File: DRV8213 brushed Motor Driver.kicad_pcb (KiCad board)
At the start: 4 copper layers, 15 x 15 mm, 27 parts, among them J1 Keystone 6102, J10 Precidip 852-10-004-20-001101, J11 Precidip 852-10-004-20-001101, J2 Keystone 6102, J3 Keystone 6100, J4 Keystone 6100, J5 Keystone 6102, J6 Keystone 6102, J7 Keystone 6100, J8 Keystone 6100, J9 JST PH 2mm horizontal, U1 DRV8213RTER, U2 LP2981-3.3

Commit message: Removed 3v3 test pad
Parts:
- removed TP2: 3v3, TestPoint:TestPoint_Pad_D1.0mm
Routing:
- net +3.3V: track 22.8 -> 21.3 mm
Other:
- board text removed: "3v3"
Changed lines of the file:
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@@
 		)
 	)
-	(footprint "TestPoint:TestPoint_Pad_D1.0mm"
-		(layer "B.Cu")
-		(at 164.8 105.675 180)
-		(descr "SMD pad as test Point, diameter 1.0mm")
-		(tags "test point SMD pad")
-		(property "Reference" "TP2"
-			(at 0 1.448 0)
-			(layer "B.SilkS")
-			(hide yes)
-			(effects
-				(font
-					(size 1 1)
-					(thickness 0.15)
-				)
-				(justify mirror)
-			)
-		)
-		(property "Value" "3v3"
-			(at 0 -1.55 0)
-			(layer "B.Fab")
-			(effects
-				(font
-					(size 1 1)
-					(thickness 0.15)
-				)
-				(justify mirror)
-			)
-		)
-		(property "Datasheet" "~"
-			(at 0 0 0)
-			(unlocked yes)
-			(layer "B.Fab")
-			(hide yes)
-			(effects
-				(font
-					(size 1.27 1.27)
-					(thickness 0.15)
-				)
-				(justify mirror)
-			)
-		)
-		(property "Description" "test point"
-			(at 0 0 0)
-			(unlocked yes)
-			(layer "B.Fab")
-			(hide yes)
-			(effects
-				(font
-					(size 1.27 1.27)
-					(thickness 0.15)
-				)
-				(justify mirror)
-			)
-		)
-		(property ki_fp_filters "Pin* Test*")
-		(sheetname "/")
-		(sheetfile "DRV8213 brushed Motor Driver.kicad_sch")
-		(attr exclude_from_pos_files exclude_from_bom)
-		(fp_circle
-			(center 0 0)
-			(end 0 -0.7)
-			(stroke
-				(width 0.12)
-				(type solid)
-			)
-			(fill no)
-			(layer "B.SilkS")
-		)
-		(fp_circle
-			(center 0 0)
-			(end 1 0)
-			(stroke
-				(width 0.05)
-				(type solid)
-			)
-			(fill no)
-			(layer "B.CrtYd")
-		)
-		(fp_text user "${REFERENCE}"
-			(at 0 1.45 0)
-			(layer "B.Fab")
-			(effects
-				(font
-					(size 1 1)
-					(thickness 0.15)
-				)
-				(justify mirror)
-			)
-		)
-		(pad "1" smd circle
-			(at 0 0 180)
-			(size 1 1)
-			(layers "B.Cu" "B.Mask")
-			(net 7 "+3.3V")
-			(pinfunction "1")
-			(pintype "passive")
-		)
-		(embedded_fonts no)
-	)
 	(footprint "Capacitor_SMD:C_0603_1608Metric"
 		(layer "B.Cu")
@@
 		)
 	)
-	(gr_text "3v3"
-		(at 165.45 106.5 90)
-		(layer "B.SilkS")
-		(effects
-			(font
-				(size 1 1)
-				(thickness 0.15)
-			)
-			(justify left bottom mirror)
-		)
-	)
 	(gr_text "⊖"
 		(at 173.937583 108.991882 0)
@@
 	)
 	(segment
-		(start 164.8 104.53)
-		(end 164.8 105.675)
-		(width 0.2)
-		(layer "B.Cu")
-		(net 7)
-	)
-	(segment
 		(start 167.1 99.65)
 		(end 167.609451 99.140549)
@@
 	)
 	(segment
-		(start 164.57 104.3)
-		(end 164.8 104.53)
-		(width 0.2)
-		(layer "B.Cu")
-		(net 7)
-	)
-	(segment
 		(start 164.55 103.55)
 		(end 164.6 103.5)
@@
 		(min_thickness 0.25)
 		(filled_areas_thickness no)
-		(fill
+		(fill yes
 			(thermal_gap 0.5)
 			(thermal_bridge_width 0.5)

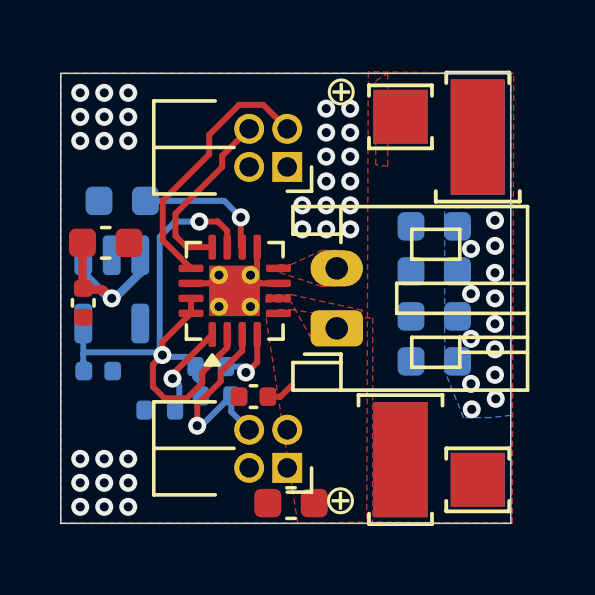
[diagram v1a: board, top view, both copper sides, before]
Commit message: Fixed connector placement
It was overlapping a whole millimeter!
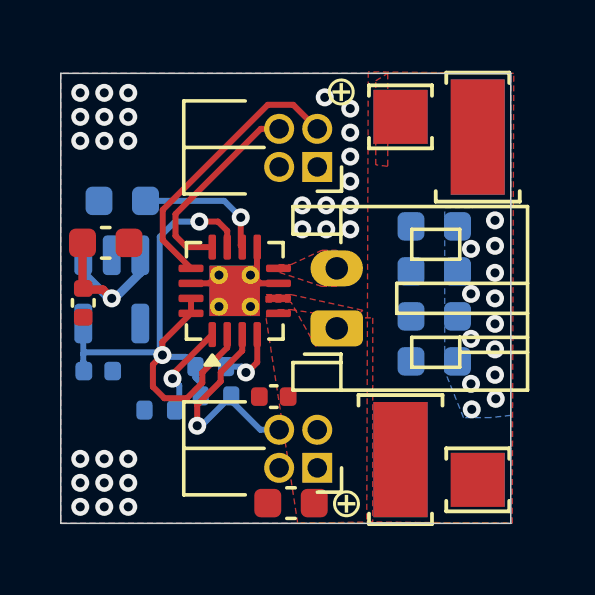
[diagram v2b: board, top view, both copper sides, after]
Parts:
- moved J10 1.00 mm to (172.3, 97.3)
- moved J11 1.00 mm to (172.3, 107.3)
- moved C6 0.68 mm to (170.9, 105.0)
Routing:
- net Fault: track 7.33 -> 8.33 mm
- net VDD: track 7.43 -> 6.48 mm
- net ADC-A: track 8.10 -> 8.98 mm
- net Stall: track 6.59 -> 7.37 mm
- net PWM-B: track 5.96 -> 6.74 mm
- net GNDPWR: vias 32 -> 29
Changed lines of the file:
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@@
 	(footprint "Capacitor_SMD:C_0402_1005Metric"
 		(layer "F.Cu")
-		(at 170.225 104.975 180)
+		(at 170.9 104.975 180)
 		(descr "Capacitor SMD 0402 (1005 Metric), square (rectangular) end terminal, IPC_7351 nominal, (Body size source: IPC-SM-782 page 76, https://www.pcb-3d.com/wordpress/wp-content/uploads/ipc-sm-782a_amendment_1_and_2.pdf), generated with kicad-footprint-generator")
 		(tags "capacitor")
@@
 	(footprint "custom_Connector:Precidip 852-10-004-20-001101"
 		(layer "F.Cu")
-		(at 171.35 97.32 180)
+		(at 172.35 97.32 180)
 		(descr "Through hole angled pin header, 2x02, 1.27mm pitch, 4.0mm pin length, double rows")
 		(tags "Through hole angled pin header THT 2x02 1.27mm double row")
@@
 	(footprint "custom_Connector:Precidip 852-10-004-20-001101"
 		(layer "F.Cu")
-		(at 171.35 107.35 180)
+		(at 172.35 107.35 180)
 		(descr "Through hole angled pin header, 2x02, 1.27mm pitch, 4.0mm pin length, double rows")
 		(tags "Through hole angled pin header THT 2x02 1.27mm double row")
@@
 	)
 	(gr_line
-		(start 170.775 108.825)
-		(end 171.325 108.025)
+		(start 171.1 108.85)
+		(end 172.125 108.05)
 		(stroke
 			(width 0.12)
@@
 	)
 	(gr_line
-		(start 171.35 105.45)
-		(end 171.425 104.6)
+		(start 172.35 105.4625)
+		(end 172.4125 104.7875)
 		(stroke
 			(width 0.12)
@@
 	)
 	(gr_line
-		(start 170.275 105.4)
+		(start 171.05 105.4)
 		(end 170.075 103.35)
 		(stroke
@@
 	)
 	(gr_text "⊕"
-		(at 172.55 109 0)
+		(at 172.75 109.1 0)
 		(layer "F.SilkS")
 		(effects
@@
 	)
 	(gr_text "Fault"
-		(at 170.75 109.1 0)
+		(at 171.075 109.125 0)
 		(layer "B.SilkS")
 		(effects
@@
 	)
 	(gr_text "PWM"
-		(at 168.075 94.225 90)
+		(at 169.675 94.325 90)
 		(layer "B.SilkS")
 		(effects
@@
 	)
 	(gr_text "A B"
-		(at 169.225 95.425 0)
+		(at 170.025 95.45 0)
 		(layer "B.SilkS")
 		(effects
@@
 	)
 	(gr_text "⊖"
-		(at 173.937583 108.991882 0)
+		(at 174.121418 109.091783 0)
 		(layer "B.SilkS")
 		(effects
@@
 	)
 	(gr_text "CSA"
-		(at 174.4 104.725 0)
+		(at 174.95 104.725 0)
 		(layer "B.SilkS")
 		(effects
@@
 		(net 1)
 	)
-	(segment
-		(start 171.125 104.975)
-		(end 171.5 104.6)
-		(width 0.2)
-		(layer "F.Cu")
-		(net 1)
-	)
-	(segment
-		(start 170.705 104.975)
-		(end 171.125 104.975)
-		(width 0.2)
-		(layer "F.Cu")
-		(net 1)
-	)
 	(via
 		(at 178.275 103.4)
@@
 	)
 	(via
-		(at 172.65 95.375)
-		(size 0.6)
-		(drill 0.3)
-		(layers "F.Cu" "B.Cu")
-		(free yes)
-		(net 2)
-	)
-	(via
-		(at 172.65 96.175)
+		(at 172.6 95)
 		(size 0.6)
 		(drill 0.3)
@@
 	)
 	(via
-		(at 172.65 96.975)
-		(size 0.6)
-		(drill 0.3)
-		(layers "F.Cu" "B.Cu")
-		(free yes)
-		(net 2)
-	)
-	(via
 		(at 165.25 95.65)
 		(size 0.6)
@@
 	)
 	(via
-		(at 172.65 97.8)
-		(size 0.6)
-		(drill 0.3)
-		(layers "F.Cu" "B.Cu")
-		(free yes)
-		(net 2)
-	)
-	(via
 		(at 173.45 98.6)
 		(size 0.6)
@@
 	)
 	(segment
-		(start 167.2 98.45)
-		(end 168.75 96.9)
-		(width 0.2)
-		(layer "F.Cu")
-		(net 6)
-	)
-	(segment
-		(start 169.748214 95.249)
-		(end 170.549 95.249)
-		(width 0.2)
-		(layer "F.Cu")
-		(net 6)
-	)
-	(segment
-		(start 167.2 99.7575)
-		(end 167.2 98.45)
+		(start 168.1425 100.7)
+		(end 167.2 99.7575)
 		(width 0.2)
 		(layer "F.Cu")
@@
 	)
 	(segment
-		(start 168.1425 100.7)
-		(end 167.2 99.7575)
+		(start 170.701 95.249)
+		(end 171.549 95.249)
 		(width 0.2)
 		(layer "F.Cu")
@@
 	)
 	(segment
-		(start 168.75 96.247214)
-		(end 169.748214 95.249)
+		(start 171.549 95.249)
+		(end 172.35 96.05)
 		(width 0.2)
 		(layer "F.Cu")
@@
 	)
 	(segment
-		(start 170.549 95.249)
-		(end 171.35 96.05)
+		(start 167.2 99.7575)
+		(end 167.2 98.75)
 		(width 0.2)
 		(layer "F.Cu")
@@
 	)
 	(segment
-		(start 168.75 96.9)
-		(end 168.75 96.247214)
+		(start 167.2 98.75)
+		(end 170.701 95.249)
 		(width 0.2)
 		(layer "F.Cu")
@@
 	)
 	(segment
-		(start 169.18 97.32)
-		(end 169.18 96.95)
+		(start 168.000686 99.9925)
+		(end 167.625 99.616814)
 		(width 0.2)
 		(layer "F.Cu")
@@
 	)
 	(segment
-		(start 169.18 96.95)
-		(end 170.08 96.05)
+		(start 170.465686 96.05)
+		(end 171.08 96.05)
 		(width 0.2)
 		(layer "F.Cu")
@@
 	)
 	(segment
-		(start 168.000686 99.9925)
-		(end 167.625 99.616814)
-		(width 0.2)
-		(layer "F.Cu")
-		(net 8)
-	)
-	(segment
-		(start 167.625 98.875)
-		(end 169.18 97.32)
+		(start 167.625 98.890686)
+		(end 170.465686 96.05)
 		(width 0.2)
 		(layer "F.Cu")
@@
 	(segment
 		(start 167.625 99.616814)
-		(end 167.625 98.875)
+		(end 167.625 98.890686)
 		(width 0.2)
 		(layer "F.Cu")
@@
 	)
 	(segment
-		(start 171.23 106.08)
-		(end 171.35 106.08)
-		(width 0.2)
-		(layer "B.Cu")
-		(net 10)
-	)
-	(segment
 		(start 167.75 104.6)
 		(end 167.525 104.375)
@@
 	)
 	(segment
-		(start 170.549 105.279)
-		(end 171.35 106.08)
+		(start 168.429 105.279)
+		(end 171.549 105.279)
 		(width 0.2)
 		(layer "In2.Cu")
@@
 	)
 	(segment
-		(start 168.429 105.279)
-		(end 170.549 105.279)
+		(start 171.549 105.279)
+		(end 172.35 106.08)
 		(width 0.2)
 		(layer "In2.Cu")
@@
 	)
 	(segment
-		(start 169.485 105.485)
-		(end 170.08 106.08)
+		(start 168.48893 105.94607)
+		(end 169.485 104.95)
 		(width 0.2)
 		(layer "B.Cu")
@@
 	)
 	(segment
-		(start 168.48893 105.94607)
-		(end 169.485 104.95)
+		(start 170.455 106.08)
+		(end 169.485 105.11)
+		(width 0.2)
+		(layer "B.Cu")
+		(net 11)
+	)
+	(segment
+		(start 171.08 106.08)
+		(end 170.455 106.08)
 		(width 0.2)
 		(layer "B.Cu")
@@
 	)
 	(segment
-		(start 169.485 104.95)
-		(end 169.485 105.485)
+		(start 169.485 105.11)
+		(end 169.485 104.95)
 		(width 0.2)
 		(layer "B.Cu")
@@
 	)
 	(segment
-		(start 169.972524 104.170466)
-		(end 169.972524 104.422524)
+		(start 173.151 106.549)
+		(end 172.35 107.35)
 		(width 0.2)
 		(layer "In2.Cu")
@@
 	)
 	(segment
-		(start 172.151 106.549)
-		(end 171.35 107.35)
+		(start 170.4 104.85)
+		(end 172.252786 104.85)
 		(width 0.2)
 		(layer "In2.Cu")
@@
 	)
 	(segment
-		(start 172.151 105.748214)
-		(end 172.151 106.549)
+		(start 172.252786 104.85)
+		(end 173.151 105.748214)
 		(width 0.2)
 		(layer "In2.Cu")
@@
 	)
 	(segment
-		(start 171.252786 104.85)
-		(end 172.151 105.748214)
+		(start 169.972524 104.422524)
+		(end 170.4 104.85)
 		(width 0.2)
 		(layer "In2.Cu")
@@
 	)
 	(segment
-		(start 169.972524 104.422524)
-		(end 170.4 104.85)
+		(start 169.972524 104.170466)
+		(end 169.972524 104.422524)
 		(width 0.2)
 		(layer "In2.Cu")
@@
 	)
 	(segment
-		(start 170.4 104.85)
-		(end 171.252786 104.85)
+		(start 173.151 105.748214)
+		(end 173.151 106.549)
 		(width 0.2)
 		(layer "In2.Cu")

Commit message: Add 1mm round corner cutouts to every edge
This is a future proofing step for an idea I had, it may not come to anything, but whatever
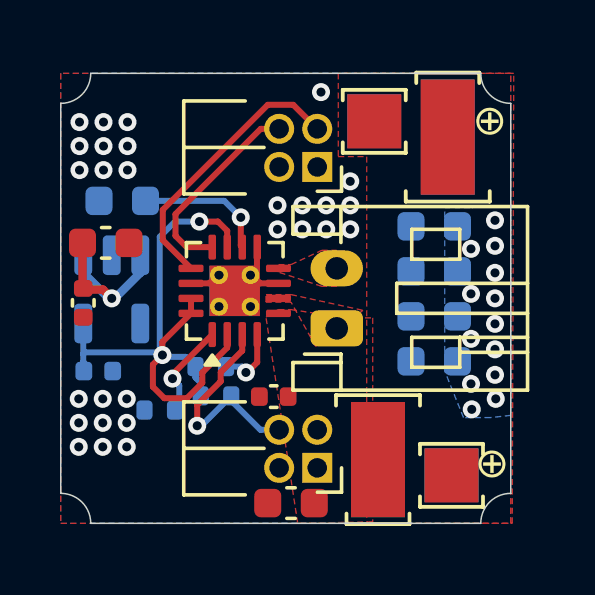
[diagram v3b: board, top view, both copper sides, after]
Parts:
- moved J2 1.00 mm to (176.7, 96.3)
- moved J6 1.00 mm to (176.7, 96.3)
- moved J3 0.89 mm to (176.8, 107.6)
- moved J7 0.89 mm to (176.8, 107.6)
- moved J4 0.89 mm to (174.2, 95.8)
- moved J8 0.89 mm to (174.2, 95.8)
- moved J1 0.75 mm to (174.4, 107.1)
- moved J5 0.75 mm to (174.4, 107.1)
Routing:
- net GNDPWR: vias 29 -> 28
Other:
- outline, holes or cut-outs redrawn
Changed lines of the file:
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@@
 	(footprint "custom_Connector:Keystone_6100"
 		(layer "F.Cu")
-		(at 177.7 107.75)
+		(at 176.825 107.6)
 		(property "Reference" "J3"
 			(at 0.3 -2.55 0)
@@
 	(footprint "custom_Connector:Keystone_6102"
 		(layer "F.Cu")
-		(at 175.125 107.075)
+		(at 174.375 107.075)
 		(property "Reference" "J1"
 			(at 1.9 -0.2 90)
@@
 	(footprint "custom_Connector:Keystone_6100"
 		(layer "F.Cu")
-		(at 175.125 95.65 180)
+		(at 174.25 95.8 180)
 		(property "Reference" "J4"
 			(at 0.3 -2.55 0)
@@
 	(footprint "custom_Connector:Keystone_6102"
 		(layer "F.Cu")
-		(at 177.7 96.325 180)
+		(at 176.7 96.325 180)
 		(property "Reference" "J2"
 			(at 1.9 -0.2 90)
@@
 	(footprint "custom_Connector:Keystone_6100"
 		(layer "B.Cu")
-		(at 175.125 95.65)
+		(at 174.25 95.8)
 		(property "Reference" "J8"
 			(at 0.3 2.55 180)
@@
 	(footprint "custom_Connector:Keystone_6102"
 		(layer "B.Cu")
-		(at 175.125 107.075 180)
+		(at 174.375 107.075 180)
 		(property "Reference" "J5"
 			(at 1.9 0.2 90)
@@
 	(footprint "custom_Connector:Keystone_6102"
 		(layer "B.Cu")
-		(at 177.7 96.325)
+		(at 176.7 96.325)
 		(property "Reference" "J6"
 			(at 1.9 0.2 90)
@@
 	(footprint "custom_Connector:Keystone_6100"
 		(layer "B.Cu")
-		(at 177.7 107.75 180)
+		(at 176.825 107.6 180)
 		(property "Reference" "J7"
 			(at 0.3 2.55 0)
@@
 		(layer "B.SilkS")
 	)
-	(gr_rect
-		(start 163.8 94.2)
-		(end 178.8 109.2)
+	(gr_arc
+		(start 178.8 95.2)
+		(mid 178.092893 94.907107)
+		(end 177.8 94.2)
+		(stroke
+			(width 0.05)
+			(type default)
+		)
+		(layer "Edge.Cuts")
+	)
+	(gr_line
+		(start 163.8 108.2)
+		(end 163.8 95.2)
+		(stroke
+			(width 0.05)
+			(type solid)
+		)
+		(layer "Edge.Cuts")
+	)
+	(gr_arc
+		(start 164.8 94.2)
+		(mid 164.507107 94.907107)
+		(end 163.8 95.2)
+		(stroke
+			(width 0.05)
+			(type default)
+		)
+		(layer "Edge.Cuts")
+	)
+	(gr_line
+		(start 177.8 109.2)
+		(end 164.8 109.2)
+		(stroke
+			(width 0.05)
+			(type solid)
+		)
+		(layer "Edge.Cuts")
+	)
+	(gr_arc
+		(start 163.8 108.2)
+		(mid 164.507107 108.492893)
+		(end 164.8 109.2)
+		(stroke
+			(width 0.05)
+			(type default)
+		)
+		(layer "Edge.Cuts")
+	)
+	(gr_line
+		(start 164.8 94.2)
+		(end 177.8 94.2)
+		(stroke
+			(width 0.05)
+			(type solid)
+		)
+		(layer "Edge.Cuts")
+	)
+	(gr_line
+		(start 178.8 95.2)
+		(end 178.8 108.2)
+		(stroke
+			(width 0.05)
+			(type solid)
+		)
+		(layer "Edge.Cuts")
+	)
+	(gr_arc
+		(start 177.8 109.2)
+		(mid 178.092893 108.492893)
+		(end 178.8 108.2)
 		(stroke
 			(width 0.05)
 			(type default)
 		)
-		(fill no)
 		(layer "Edge.Cuts")
 	)
 	(gr_text "⊕"
-		(at 172.575 95.375 0)
+		(at 177.525 96.35 0)
 		(layer "F.SilkS")
 		(effects
@@
 	)
 	(gr_text "⊕"
-		(at 172.75 109.1 0)
+		(at 177.6 107.775 0)
 		(layer "F.SilkS")
 		(effects
@@
 	)
 	(gr_text "⊖"
-		(at 174.121418 109.091783 0)
+		(at 177.375 106.3 0)
 		(layer "B.SilkS")
 		(effects
@@
 	)
 	(gr_text "⊖"
-		(at 173.967836 95.373351 0)
+		(at 174.925 98.025 0)
 		(layer "B.SilkS")
 		(effects
@@
 		)
 	)
-	(gr_text_box "The connectors you see sticking off the edge of the board are going to be cut in half, I don't need maximum capability, and I want to save space and cost"
-		(start 167.35 98.5)
-		(end 177.15 105.6)
-		(margins 0.425 0.425 0.425 0.425)
-		(layer "Cmts.User")
-		(effects
-			(font
-				(size 0.5 0.5)
-				(thickness 0.125)
-			)
-			(justify left top)
-		)
-		(border yes)
-		(stroke
-			(width 0.1)
-			(type solid)
-		)
-	)
 	(segment
 		(start 164.709886 101.409886)
@@
 	)
 	(via
-		(at 173.45 95.375)
-		(size 0.6)
-		(drill 0.3)
-		(layers "F.Cu" "B.Cu")
-		(free yes)
-		(net 2)
-	)
-	(via
-		(at 172.6 95)
+		(at 173.45 97.8)
 		(size 0.6)
 		(drill 0.3)
@@
 	)
 	(via
-		(at 173.45 96.975)
+		(at 165.2 105.85)
 		(size 0.6)
 		(drill 0.3)
@@
 	)
 	(via
-		(at 173.45 97.8)
+		(at 166 105.05)
 		(size 0.6)
 		(drill 0.3)
@@
 	)
 	(via
-		(at 165.25 107.85)
+		(at 166 105.85)
 		(size 0.6)
 		(drill 0.3)
@@
 	)
 	(via
-		(at 166.05 107.05)
+		(at 166 106.65)
 		(size 0.6)
 		(drill 0.3)
@@
 	)
 	(via
-		(at 166.05 107.85)
+		(at 165.225 96.625)
 		(size 0.6)
 		(drill 0.3)
@@
 	)
 	(via
-		(at 166.05 108.65)
+		(at 166.025 97.425)
 		(size 0.6)
 		(drill 0.3)
@@
 	)
 	(via
-		(at 165.25 95.65)
+		(at 164.4 106.65)
 		(size 0.6)
 		(drill 0.3)
@@
 	)
 	(via
-		(at 166.05 96.45)
+		(at 164.4 105.85)
 		(size 0.6)
 		(drill 0.3)
@@
 	)
 	(via
-		(at 164.45 108.65)
+		(at 164.425 97.425)
 		(size 0.6)
 		(drill 0.3)
@@
 	)
 	(via
-		(at 164.45 107.85)
+		(at 172.65 99.4)
 		(size 0.6)
 		(drill 0.3)
@@
 	)
 	(via
-		(at 164.45 96.45)
+		(at 172.65 98.6)
 		(size 0.6)
 		(drill 0.3)
@@
 	)
 	(via
-		(at 172.65 99.4)
+		(at 164.4 105.05)
 		(size 0.6)
 		(drill 0.3)
@@
 	)
 	(via
-		(at 172.65 98.6)
+		(at 166.025 95.825)
 		(size 0.6)
 		(drill 0.3)
@@
 	)
 	(via
-		(at 164.45 107.05)
+		(at 165.2 106.65)
 		(size 0.6)
 		(drill 0.3)
@@
 	)
 	(via
-		(at 166.05 94.85)
+		(at 173.45 98.6)
 		(size 0.6)
 		(drill 0.3)
@@
 	)
 	(via
-		(at 165.25 108.65)
+		(at 164.425 96.625)
 		(size 0.6)
 		(drill 0.3)
@@
 	)
 	(via
-		(at 173.45 98.6)
+		(at 166.025 96.625)
 		(size 0.6)
 		(drill 0.3)
@@
 	)
 	(via
-		(at 164.45 95.65)
+		(at 171.025 99.4)
 		(size 0.6)
 		(drill 0.3)
@@
 	)
 	(via
-		(at 166.05 95.65)
+		(at 171.85 98.6)
 		(size 0.6)
 		(drill 0.3)
@@
 	)
 	(via
-		(at 171.85 98.6)
+		(at 173.45 99.4)
 		(size 0.6)
 		(drill 0.3)
@@
 	)
 	(via
-		(at 173.45 96.175)
+		(at 164.425 95.825)
 		(size 0.6)
 		(drill 0.3)
@@
 	)
 	(via
-		(at 173.45 99.4)
+		(at 171.85 99.4)
 		(size 0.6)
 		(drill 0.3)
@@
 	)
 	(via
-		(at 164.45 94.85)
+		(at 171.025 98.6)
 		(size 0.6)
 		(drill 0.3)
@@
 	)
 	(via
-		(at 171.85 99.4)
+		(at 165.225 95.825)
 		(size 0.6)
 		(drill 0.3)
@@
 	)
 	(via
-		(at 165.25 94.85)
+		(at 165.2 105.05)
 		(size 0.6)
 		(drill 0.3)
@@
 	)
 	(via
-		(at 165.25 107.05)
+		(at 165.225 97.425)
 		(size 0.6)
 		(drill 0.3)
@@
 	)
 	(via
-		(at 165.25 96.45)
+		(at 172.475 94.825)
 		(size 0.6)
 		(drill 0.3)
@@
 		(polygon
 			(pts
-				(xy 178.85 109.2) (xy 178.9 94.2) (xy 174.05 94.15) (xy 174 109.15)
-			)
-		)
-	)
-	(zone
-		(net 1)
-		(net_name "VDD")
-		(layer "F.Cu")
-		(hatch edge 0.5)
-		(connect_pads yes
-			(clearance 0.2)
-		)
-		(min_thickness 0.2)
-		(filled_areas_thickness no)
-		(fill yes
-			(thermal_gap 0.5)
-			(thermal_bridge_width 0.5)
-		)
-		(polygon
-			(pts
-				(xy 174.299999 94.45) (xy 174.7 94.2) (xy 174.7 97.3) (xy 174.299999 97.25)
+				(xy 178.85 109.2) (xy 178.9 94.2) (xy 173.05 94.2) (xy 173.05 96.975) (xy 174 96.975) (xy 174 109.2)
 			)
 		)
@@
 		(polygon
 			(pts
-				(xy 174.2 96.875) (xy 176.45 96.875) (xy 176.45 98.55) (xy 178.6 98.55) (xy 178.6 106.475) (xy 176.425 106.475)
-				(xy 176.425 104.825) (xy 174.2 104.825)
+				(xy 173.375 103.6) (xy 174.2 103.6) (xy 174.2 96.975) (xy 175.5 96.975) (xy 175.5 98.55) (xy 178.6 98.55)
+				(xy 178.6 106.4) (xy 175.625 106.4) (xy 175.625 104.825) (xy 173.375 104.825)
 			)
 		)

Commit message: Fixed connector alignment
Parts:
- moved J1 0.12 mm to (174.2, 107.1)
- moved J3 0.12 mm to (176.7, 107.6)
- moved J5 0.12 mm to (174.2, 107.1)
- moved J7 0.12 mm to (176.7, 107.6)
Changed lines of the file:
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@@
 	(footprint "custom_Connector:Keystone_6100"
 		(layer "F.Cu")
-		(at 176.825 107.6)
+		(at 176.7 107.6)
 		(property "Reference" "J3"
 			(at 0.3 -2.55 0)
@@
 	(footprint "custom_Connector:Keystone_6102"
 		(layer "F.Cu")
-		(at 174.375 107.075)
+		(at 174.25 107.075)
 		(property "Reference" "J1"
 			(at 1.9 -0.2 90)
@@
 	(footprint "custom_Connector:Keystone_6102"
 		(layer "B.Cu")
-		(at 174.375 107.075 180)
+		(at 174.25 107.075 180)
 		(property "Reference" "J5"
 			(at 1.9 0.2 90)
@@
 	(footprint "custom_Connector:Keystone_6100"
 		(layer "B.Cu")
-		(at 176.825 107.6 180)
+		(at 176.7 107.6 180)
 		(property "Reference" "J7"
 			(at 0.3 2.55 0)
